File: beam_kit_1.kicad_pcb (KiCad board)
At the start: 2 copper layers, 145 x 96 mm, 266 parts, among them J1 PZ2.54-2*20, J10 UART_SEPARATOR, J11 NRF, J12 BTN_KNOB, J13 BTN_KNOB, J14 KNOB_AND_WS, J15 dbg, J16 dbg, J17 dbg, J18 dbg, J19 SONAR, J2 PZ2.54-2*20, J20 micro_sd, J21 NRF_24_socket, J22 SSD1306_128x32_OLED, J23 3V3, J24 GND, J25 5V, J26 EXP-A, J27 PJ-320D, J28 screw_term, J29 screw_term, J3 USB_C_Receptacle, J30 RS485, J32 AUDIO, J4 probe_debug, J5 Micro_SD_Card, J6 OLED I2C, J7 VL53_PINS, J8 HC-SR04, J9 I2C, SW1 BOOTSEL, SW2 RUN, SW4 BTN1, SW5 BTN0, SW6 BTN2, SW7 RUN, U1 LIS3DH, U10 SHT30-DIS, U11 AMS1117-3.3, U12 SN74LVC1G14DBV, U13 SN74LVC1G14DBV, U14 MAX485E, U16 LMV358IDR, U2 APDS-9306-065, U3 SN74LVC1G14DBV, U4 M24256-BR, U5 RP2040, U6 SN74LVC1G14DBV, U7 W25Q16JVSS, U8 MT3608, U9 VL53L0CXV0DH1, Y1 12 MHz

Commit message: layout done
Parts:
- removed J26: EXP-A, Connector_PinHeader_2.54mm:PinHeader_1x06_P2.54mm_Vertical
- removed J31: ~, Connector_PinSocket_2.54mm:PinSocket_1x06_P2.54mm_Vertical
- removed kibuzzard-67BB32E4: G***, kibuzzard-67BB32E4
- added G***: LOGO, LOGO, B.Cu at (106.5, 105.3)
- added J33: EXP, Connector_PinHeader_2.54mm:PinHeader_1x08_P2.54mm_Vertical, F.Cu at (123.7, 58.3)
- added J34: EXP, Connector_PinSocket_2.54mm:PinSocket_1x08_P2.54mm_Vertical, F.Cu at (123.7, 53.7)
- added kibuzzard-62ECE595: G***, kibuzzard-62ECE595, B.Cu at (103.4, 120.3)
- added kibuzzard-67BB3583: G***, kibuzzard-67BB3583, F.Cu at (186.7, 77.8)
- added kibuzzard-67BB3747: G***, kibuzzard-67BB3747, F.Cu at (109.1, 89.8)
- added kibuzzard-67BB3BA0: G***, kibuzzard-67BB3BA0, F.Cu at (116.8, 61.1)
- added kibuzzard-67BB3D27: G***, kibuzzard-67BB3D27, F.Cu at (151.1, 106.3)
- moved U9 149.9 mm to (105.4, 113.8), turned to 0 degrees
- moved C57 149.7 mm to (101.3, 112.9), turned to -90 degrees
- moved JP5 148.5 mm to (112.2, 107.8), turned to 90 degrees
- moved U2 148.3 mm to (106.6, 97.3), turned to 0 degrees
- moved C56 147.4 mm to (103.8, 110.7)
- moved U4 146.4 mm to (105.4, 104.7), turned to 0 degrees
- moved U1 142.6 mm to (113.7, 104.0), turned to 0 degrees
- moved C3 142.5 mm to (110.2, 103.6)
- moved C1 142.2 mm to (103.8, 97.3)
- moved U10 141.7 mm to (113.4, 96.6)
- moved C53 138.2 mm to (114.2, 107.6), turned to -90 degrees
- moved R23 137.5 mm to (110.8, 112.7)
- moved R24 137.5 mm to (110.8, 115.0)
- moved C54 136.0 mm to (115.8, 107.6), turned to -90 degrees
- moved C55 133.2 mm to (116.0, 96.6), turned to 90 degrees
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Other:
- board text added: "ACC."
- board text added: "Designed by: Jakub Mnich (jakub.mnich@pwr.edu.pl) Krzysztof Urbanski (krzysztof.urbanski@pwr.edu.pl) 02.2025"
- board text added: "EEPROM"
- board text added: "GP1"
- board text added: "LIGHT SENSOR"
- board text added: "TEMP&RH"
- board text added: "VL53L0X"
- board text added: "XS"
- board text removed: "GPIO0"
- board text removed: "GPIO1"
- board text removed: "HAT SOCKET"

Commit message: codes and fixes
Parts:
- removed kibuzzard-67BB2D66: G***, kibuzzard-67BB2D66
- added kibuzzard-67BB4182: G***, kibuzzard-67BB4182, F.Cu at (169.1, 128.4)
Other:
- board text added: "5V"

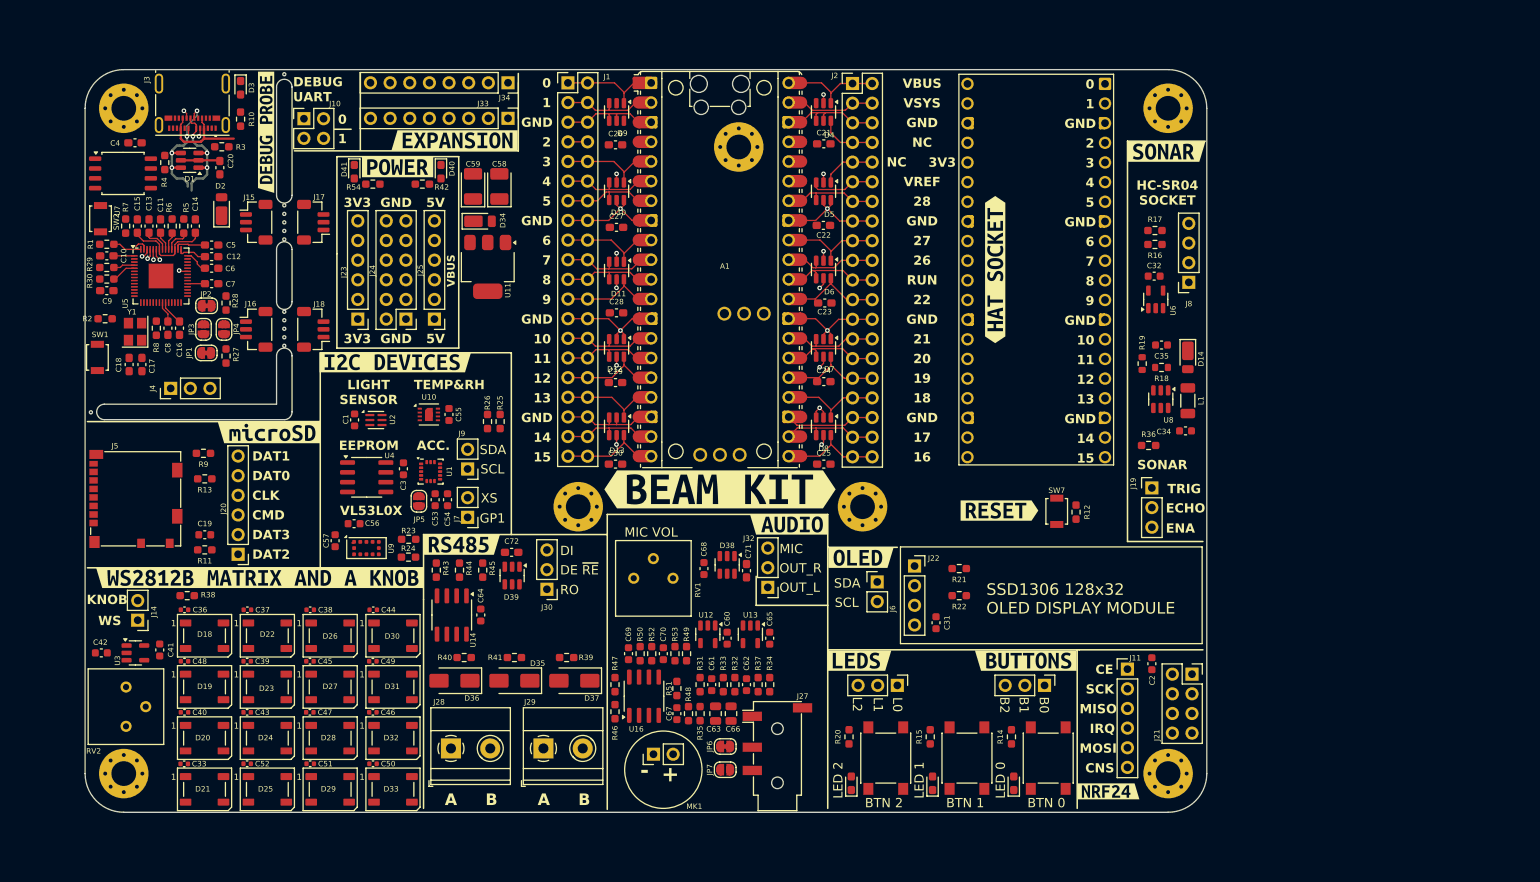
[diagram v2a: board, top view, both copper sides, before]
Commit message: RS leds fix
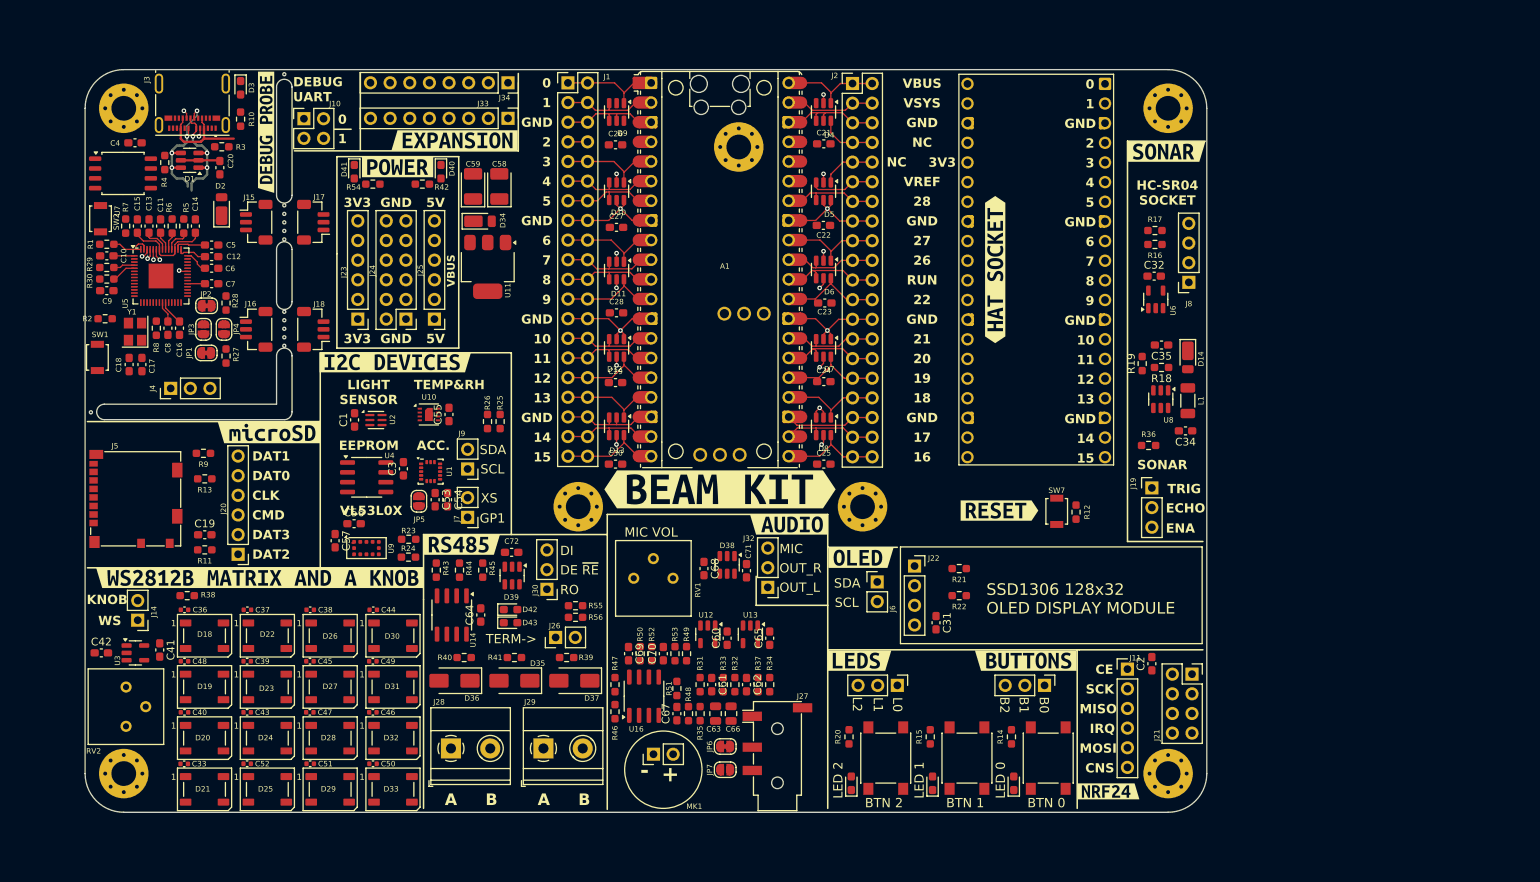
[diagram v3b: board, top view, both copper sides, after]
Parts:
- added D42: LED R, LED_SMD:LED_0603_1608Metric_Pad1.05x0.95mm_HandSolder, F.Cu at (124.0, 121.8)
- added D43: LED R, LED_SMD:LED_0603_1608Metric_Pad1.05x0.95mm_HandSolder, F.Cu at (124.0, 123.5)
- added J26: TERM, Connector_PinHeader_2.54mm:PinHeader_1x02_P2.54mm_Vertical, F.Cu at (129.8, 125.4)
- added R55: 5k1 1%, Resistor_SMD:R_0603_1608Metric_Pad0.98x0.95mm_HandSolder, F.Cu at (132.4, 121.3)
- added R56: 5k1 1%, Resistor_SMD:R_0603_1608Metric_Pad0.98x0.95mm_HandSolder, F.Cu at (132.4, 122.8)
- C1, C19, C2, C3, C31, C32, C34, C35, C41, C42, C53, C54, C55, C56, C57, C60, C61, C62, C64, C65, C67, C68, C69, C70: footprint Capacitor_SMD:C_0603_1608Metric -> Capacitor_SMD:C_0603_1608Metric_Pad1.08x0.95mm_HandSolder
- C33, C36, C37, C38, C39, C40, C43, C44, C45, C46, C47, C48, C49, C50, C51, C52: value 100n 50V -> 100n 16V
- D14, D2, D34: value 1A, 30V -> 2A, 30V
- R18, R19: footprint Resistor_SMD:R_0603_1608Metric -> Resistor_SMD:R_0603_1608Metric_Pad0.98x0.95mm_HandSolder
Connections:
- R41 pad 2: /peripheral2/B -> Net-(J26-Pin_1)
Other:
- board text added: "TERM->"

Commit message: routing in progress
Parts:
- removed the H6 at (94.8, 71.8)
- removed the H6 at (94.8, 69.5)
- removed the H6 at (94.8, 70.7)
- removed kibuzzard-67BB3583: G***, kibuzzard-67BB3583
- added H6: MB template, MountingHole:MountingHole_2.1mm, F.Cu at (94.8, 69.7)
- added kibuzzard-67BB581A: G***, kibuzzard-67BB581A, F.Cu at (192.0, 78.0)
- moved C28 2.11 mm to (136.5, 81.7), turned to 90 degrees
- moved C25 1.48 mm to (163.4, 102.0), turned to 90 degrees
- moved C57 1.30 mm to (101.3, 111.6), turned to 90 degrees
- moved C30 1.26 mm to (136.8, 102.0), turned to 90 degrees
- moved C29 1.20 mm to (136.5, 91.9), turned to 90 degrees
- moved C23 1.08 mm to (163.6, 81.8), turned to 90 degrees
- moved C22 1.08 mm to (163.5, 71.6), turned to 90 degrees
- moved C24 0.90 mm to (163.7, 91.9), turned to 90 degrees
- moved C21 0.80 mm to (163.8, 61.2), turned to 90 degrees
- moved D34 0.75 mm to (120.8, 71.6)
- moved C27 0.64 mm to (138.2, 72.0), turned to 90 degrees
- moved SW2 0.50 mm to (70.5, 71.2)
- moved C26 0.37 mm to (137.2, 61.7), turned to 90 degrees
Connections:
- D19 pad 4: Net-(D18-DOUT) -> Net-(D19-DIN)
- D20 pad 4: Net-(D19-DOUT) -> Net-(D20-DIN)
- D21 pad 4: Net-(D20-DOUT) -> Net-(D21-DIN)
- D22 pad 4: Net-(D21-DOUT) -> Net-(D18-DOUT)
- D23 pad 4: Net-(D22-DOUT) -> Net-(D19-DOUT)
- D24 pad 4: Net-(D23-DOUT) -> Net-(D20-DOUT)
- D25 pad 4: Net-(D24-DOUT) -> Net-(D21-DOUT)
- D26 pad 4: Net-(D25-DOUT) -> Net-(D22-DOUT)
- D27 pad 4: Net-(D27-DIN) -> Net-(D23-DOUT)
- D28 pad 4: Net-(D26-DOUT) -> Net-(D24-DOUT)
- D29 pad 4: Net-(D27-DOUT) -> Net-(D25-DOUT)
- D30 pad 2: Net-(D30-DOUT) -> Net-(D19-DIN)
- D30 pad 4: Net-(D28-DOUT) -> Net-(D26-DOUT)
- D31 pad 2: Net-(D31-DOUT) -> Net-(D20-DIN)
- D31 pad 4: Net-(D29-DOUT) -> Net-(D27-DOUT)
- D32 pad 2: Net-(D27-DIN) -> Net-(D21-DIN)
- D32 pad 4: Net-(D30-DOUT) -> Net-(D28-DOUT)
- D33 pad 4: Net-(D31-DOUT) -> Net-(D29-DOUT)
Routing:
- net GND: track 132.7 -> 1047.2 mm, vias 16 -> 70
- net VBUS: track 13.2 -> 498.6 mm, vias 0 -> 18
- net +3.3V: track 24.7 -> 152.6 mm, vias 0 -> 2
- net +3V3: track 0.00 -> 120.6 mm, vias 0 -> 5
- net /GPIO2: track 2.54 -> 74.9 mm
- net /GPIO9: track 13.0 -> 76.2 mm
- net /GPIO3: track 13.3 -> 74.4 mm
- net /GPIO0: track 13.2 -> 73.8 mm
- net /GPIO7: track 12.7 -> 73.1 mm
- net /GPIO10: track 12.5 -> 73.0 mm
- net /GPIO12: track 13.2 -> 73.6 mm
- net /GPIO4: track 12.6 -> 72.9 mm
- net /GPIO1: track 12.5 -> 72.7 mm
- net /GPIO15: track 13.2 -> 73.4 mm
- net /GPIO11: track 12.6 -> 72.2 mm
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
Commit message: layout done
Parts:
- added C73: 100u 6V3 Tantal, Capacitor_Tantalum_SMD:CP_EIA-3528-21_Kemet-B_Pad1.50x2.35mm_HandSolder, F.Cu at (91.6, 78.8)
- added R57: 1Meg 1%, Resistor_SMD:R_0603_1608Metric_Pad0.98x0.95mm_HandSolder, F.Cu at (75.5, 89.0)
- moved C17 1.33 mm to (76.3, 91.5)
- moved C18 1.33 mm to (74.7, 91.5)
- moved R2 1.27 mm to (70.4, 83.8), turned to -90 degrees
- moved R3 0.18 mm to (86.8, 62.0)
- moved R51 0.10 mm to (145.5, 131.9)
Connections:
- A1 pad 30: Net-(A1-RUN) -> /RUN
- C1 pad 1: +3V3 -> +3.3V
- C19 pad 1: +3V3 -> +3.3V
- C2 pad 2: +3V3 -> +3.3V
- C3 pad 2: +3V3 -> +3.3V
- C31 pad 1: +3V3 -> +3.3V
- C34 pad 1: +3V3 -> +3.3V
- C53 pad 1: +3V3 -> +3.3V
- C54 pad 1: +3V3 -> +3.3V
- C55 pad 1: +3V3 -> +3.3V
- C56 pad 1: +3V3 -> +3.3V
- C57 pad 1: +3V3 -> +3.3V
- J21 pad 1: +3V3 -> +3.3V
- J22 pad 3: +3V3 -> +3.3V
- J23 pad 1: +3V3 -> +3.3V
- J23 pad 2: +3V3 -> +3.3V
- J23 pad 3: +3V3 -> +3.3V
- J23 pad 4: +3V3 -> +3.3V
- J23 pad 5: +3V3 -> +3.3V
- J23 pad 6: +3V3 -> +3.3V
- J5 pad 4: +3V3 -> +3.3V
- L1 pad 1: +3V3 -> +3.3V
- R11 pad 2: +3V3 -> +3.3V
- R12 pad 1: Net-(A1-RUN) -> /RUN
- R21 pad 1: +3V3 -> +3.3V
- R22 pad 1: +3V3 -> +3.3V
- R23 pad 2: +3V3 -> +3.3V
- R24 pad 2: +3V3 -> +3.3V
- R25 pad 1: +3V3 -> +3.3V
- R26 pad 1: +3V3 -> +3.3V
- R36 pad 1: +3V3 -> +3.3V
- R38 pad 1: +3V3 -> +3.3V
- R54 pad 2: +3V3 -> +3.3V
- R9 pad 2: +3V3 -> +3.3V
- RV2 pad 1: +3V3 -> +3.3V
- SW7 pad 2: Net-(A1-RUN) -> /RUN
- U1 pad 1: +3V3 -> +3.3V
- U1 pad 14: +3V3 -> +3.3V
- U1 pad 8: +3V3 -> +3.3V
- U10 pad 5: +3V3 -> +3.3V
- U2 pad 3: +3V3 -> +3.3V
- U4 pad 8: +3V3 -> +3.3V
- U8 pad 5: +3V3 -> +3.3V
- U9 pad 1: +3V3 -> +3.3V
- U9 pad 11: +3V3 -> +3.3V
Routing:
- net GND: track 1047.2 -> 1677.6 mm, vias 70 -> 626
- net +3.3V: track 152.6 -> 698.1 mm, vias 2 -> 43
- net +3V3: track 120.6 -> 0.00 mm, vias 5 -> 0
- net /SWDIO: track 53.2 -> 128.4 mm, vias 2 -> 3
- net /SWCLK: track 53.4 -> 125.2 mm, vias 2 -> 3
- net /RUN: track 25.2 -> 64.9 mm
- net /prog/TARGET_TX: track 10.5 -> 47.0 mm, vias 0 -> 1
- net /GPIO1: track 72.7 -> 106.2 mm
- net /GPIO0: track 73.8 -> 107.3 mm
- net VBUS: track 498.6 -> 530.5 mm
- net Net-(U5-RUN): track 5.06 -> 33.9 mm, vias 2 -> 4
- net /prog/TARGET_RX: track 10.6 -> 38.0 mm, vias 0 -> 1
- net Net-(JP2-A): track 0.00 -> 25.8 mm, vias 0 -> 4
- net Net-(U5-GPIO25): track 1.13 -> 24.3 mm, vias 1 -> 2
- net Net-(JP1-A): track 0.00 -> 21.7 mm, vias 0 -> 2
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- added copper zone on B.Cu, net +3.3V
- added copper zone on F.Cu, net +3.3V
- added copper zone on B.Cu, net GND
- added copper zone on F.Cu, net GND
